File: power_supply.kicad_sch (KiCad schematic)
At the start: 37 parts, among them CON1 USB_B_Micro, CON2 Barrel_Jack_MountingPin, Q1 AO3401A, U1 AP1117-33, U2 AP6503, U3 CP2102N

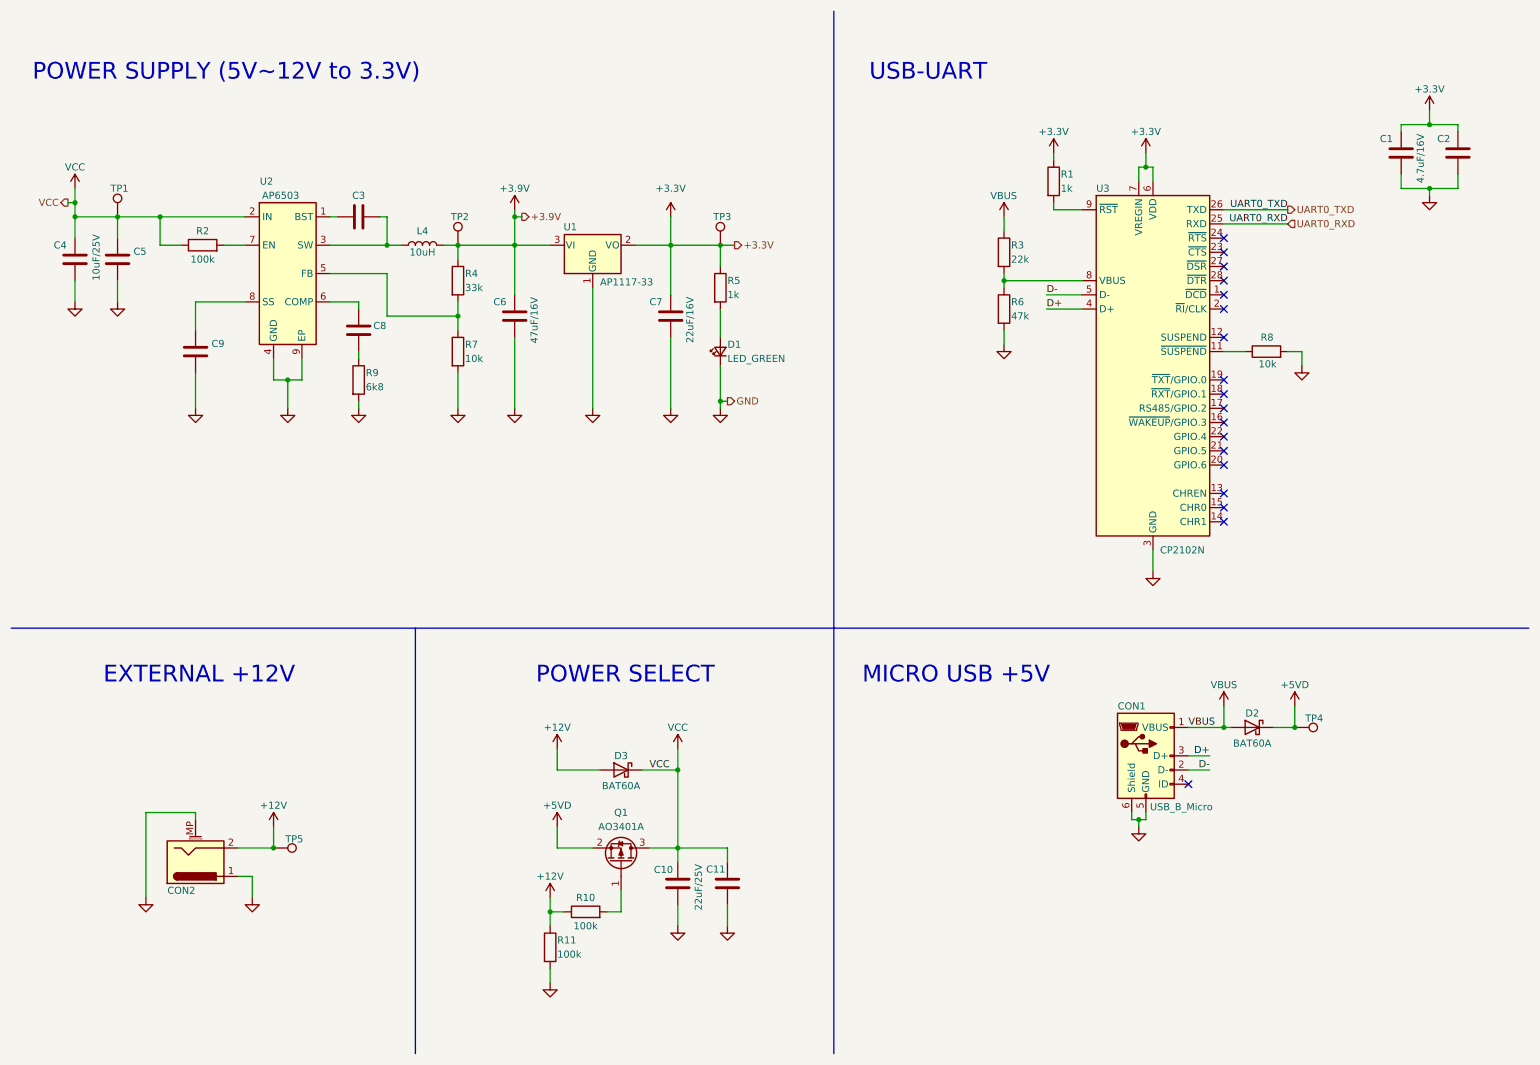
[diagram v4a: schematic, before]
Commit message: Adicionado os pads dos Test Point e alterado o Bead
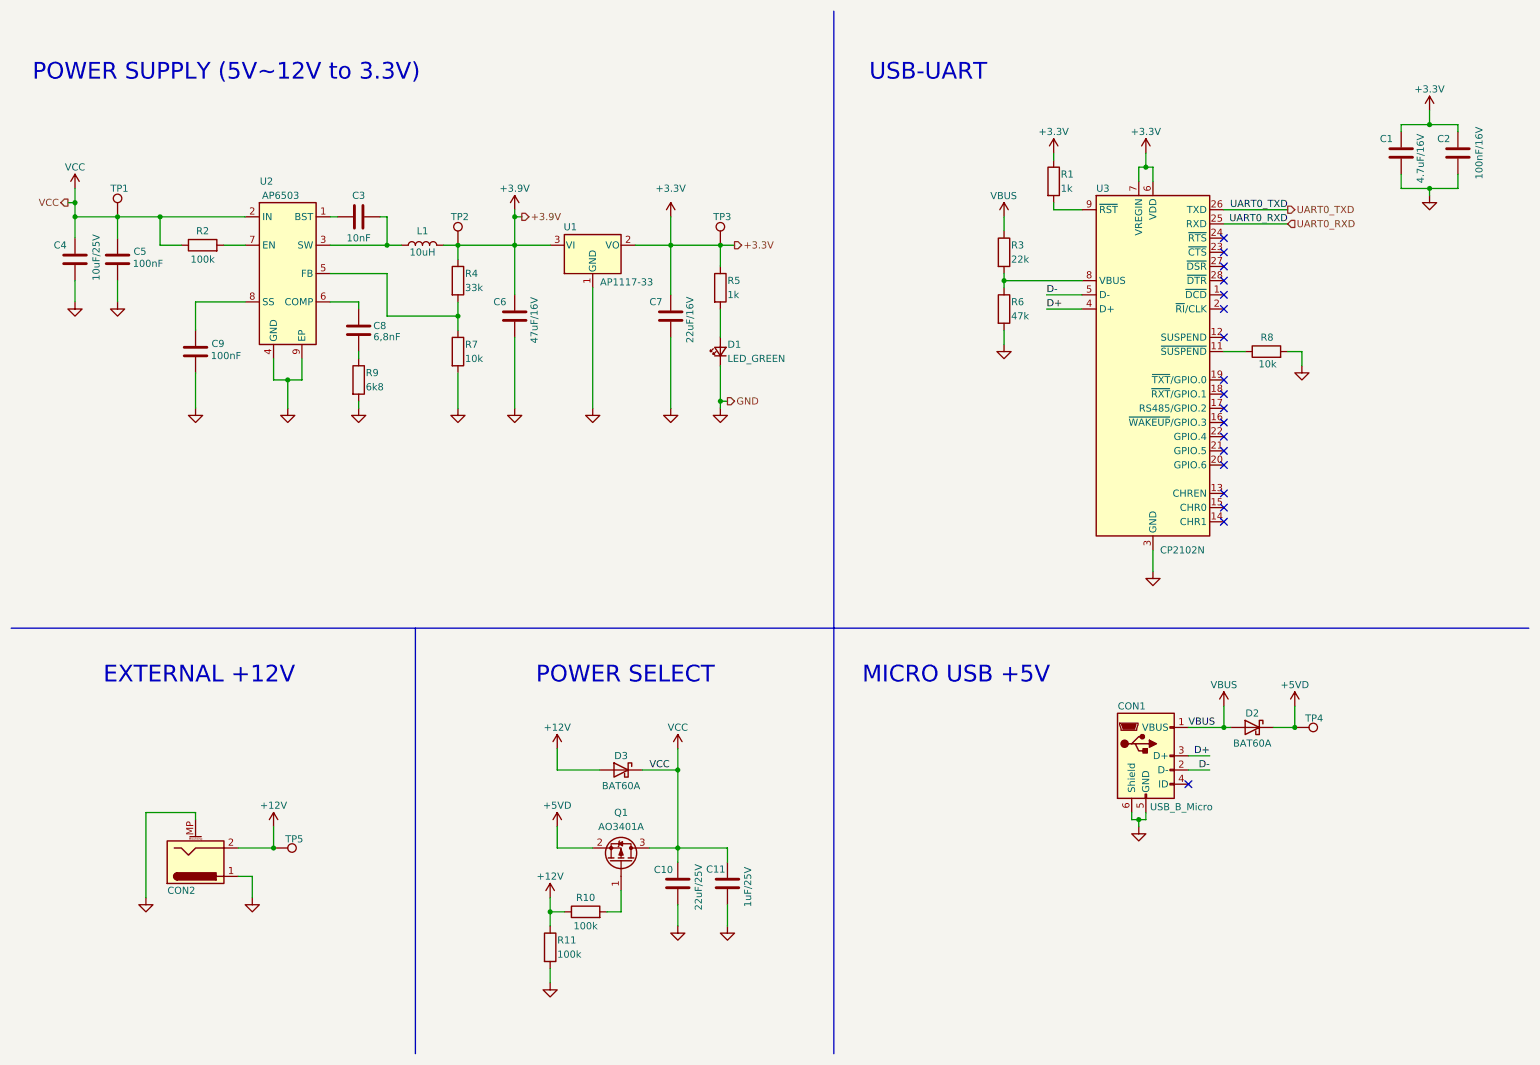
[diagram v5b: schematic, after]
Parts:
- C11: value (none) -> 1uF/25V; footprint (none) -> Capacitor_SMD:C_0603_1608Metric_Pad1.08x0.95mm_HandSolder
- C2: value (none) -> 100nF/16V; footprint (none) -> Capacitor_SMD:C_0603_1608Metric_Pad1.08x0.95mm_HandSolder
- C3: value (none) -> 10nF; footprint (none) -> Capacitor_SMD:C_0603_1608Metric_Pad1.08x0.95mm_HandSolder
- C5, C9: value (none) -> 100nF; footprint (none) -> Capacitor_SMD:C_0603_1608Metric_Pad1.08x0.95mm_HandSolder
- C8: value (none) -> 6,8nF; footprint (none) -> Capacitor_SMD:C_0603_1608Metric_Pad1.08x0.95mm_HandSolder
- TP1, TP2, TP3, TP4, TP5: value TestPoint -> (none)
- renumbered L4 to L1
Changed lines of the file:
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@@
       (effects (font (size 1.27 1.27)) (justify left))
     )
-    (property "Value" "TestPoint" (id 1) (at 142.24 51.3079 0)
+    (property "Value" "" (id 1) (at 142.24 51.3079 0)
       (effects (font (size 1.27 1.27)) (justify left) hide)
     )
@@
   (symbol (lib_id "Device:L") (at 86.36 53.34 90) (unit 1)
     (in_bom yes) (on_board yes)
-    (property "Reference" "L4" (id 0) (at 86.36 50.8 90))
+    (property "Reference" "L1" (id 0) (at 86.36 50.8 90))
     (property "Value" "10uH" (id 1) (at 86.36 54.61 90))
     (property "Footprint" "Inductor_SMD:L_Bourns-SRN8040_8x8.15mm" (id 2) (at 86.36 53.34 0)
@@
       (effects (font (size 1.27 1.27)) (justify left))
     )
-    (property "Value" "" (id 1) (at 144.632 171.8591 90)
-      (effects (font (size 1.27 1.27)) (justify left))
-    )
-    (property "Footprint" "" (id 2) (at 141.9352 171.45 0)
+    (property "Value" "1uF/25V" (id 1) (at 144.632 171.8591 90)
+      (effects (font (size 1.27 1.27)) (justify left))
+    )
+    (property "Footprint" "Capacitor_SMD:C_0603_1608Metric_Pad1.08x0.95mm_HandSolder" (id 2) (at 141.9352 171.45 0)
       (effects (font (size 1.27 1.27)) hide)
     )
@@
     (in_bom yes) (on_board yes)
     (property "Reference" "C2" (id 0) (at 269.24 34.29 0))
-    (property "Value" "" (id 1) (at 275.59 36.83 90))
-    (property "Footprint" "" (id 2) (at 270.8148 33.02 0)
+    (property "Value" "100nF/16V" (id 1) (at 275.59 36.83 90))
+    (property "Footprint" "Capacitor_SMD:C_0603_1608Metric_Pad1.08x0.95mm_HandSolder" (id 2) (at 270.8148 33.02 0)
       (effects (font (size 1.27 1.27)) hide)
     )
@@
       (effects (font (size 1.27 1.27)) (justify left))
     )
-    (property "Value" "TestPoint" (id 1) (at 34.29 46.2279 0)
+    (property "Value" "" (id 1) (at 34.29 46.2279 0)
       (effects (font (size 1.27 1.27)) (justify left) hide)
     )
@@
     (in_bom yes) (on_board yes)
     (property "Reference" "C3" (id 0) (at 74.93 44.45 90))
-    (property "Value" "" (id 1) (at 74.93 52.07 90))
-    (property "Footprint" "" (id 2) (at 78.74 47.2948 0)
+    (property "Value" "10nF" (id 1) (at 74.93 52.07 90))
+    (property "Footprint" "Capacitor_SMD:C_0603_1608Metric_Pad1.08x0.95mm_HandSolder" (id 2) (at 78.74 47.2948 0)
       (effects (font (size 1.27 1.27)) hide)
     )
@@
     (in_bom yes) (on_board yes)
     (property "Reference" "C5" (id 0) (at 35.7705 54.4674 0))
-    (property "Value" "" (id 1) (at 37.2006 56.6367 0))
-    (property "Footprint" "" (id 2) (at 30.7848 52.07 0)
+    (property "Value" "100nF" (id 1) (at 37.2006 56.6367 0))
+    (property "Footprint" "Capacitor_SMD:C_0603_1608Metric_Pad1.08x0.95mm_HandSolder" (id 2) (at 30.7848 52.07 0)
       (effects (font (size 1.27 1.27)) hide)
     )
@@
       (effects (font (size 1.27 1.27)) (justify left))
     )
-    (property "Value" "" (id 1) (at 77.5519 69.7652 0)
-      (effects (font (size 1.27 1.27)) (justify left))
-    )
-    (property "Footprint" "" (id 2) (at 75.8952 72.39 0)
+    (property "Value" "6,8nF" (id 1) (at 77.5519 69.7652 0)
+      (effects (font (size 1.27 1.27)) (justify left))
+    )
+    (property "Footprint" "Capacitor_SMD:C_0603_1608Metric_Pad1.08x0.95mm_HandSolder" (id 2) (at 75.8952 72.39 0)
       (effects (font (size 1.27 1.27)) hide)
     )
@@
       (effects (font (size 1.27 1.27)) (justify left))
     )
-    (property "Value" "TestPoint" (id 1) (at 244.6021 142.24 0)
+    (property "Value" "" (id 1) (at 244.6021 142.24 0)
       (effects (font (size 1.27 1.27)) (justify left) hide)
     )
@@
       (effects (font (size 1.27 1.27)) (justify left))
     )
-    (property "Value" "TestPoint" (id 1) (at 61.7221 163.83 0)
+    (property "Value" "" (id 1) (at 61.7221 163.83 0)
       (effects (font (size 1.27 1.27)) (justify left) hide)
     )
@@
       (effects (font (size 1.27 1.27)) (justify left))
     )
-    (property "Value" "TestPoint" (id 1) (at 95.25 51.3079 0)
+    (property "Value" "" (id 1) (at 95.25 51.3079 0)
       (effects (font (size 1.27 1.27)) (justify left) hide)
     )
@@
     (in_bom yes) (on_board yes)
     (property "Reference" "C9" (id 0) (at 49.7405 70.9774 0))
-    (property "Value" "" (id 1) (at 51.1706 73.1467 0))
-    (property "Footprint" "" (id 2) (at 44.7548 68.58 0)
-      (effects (font (size 1.27 1.27)) hide)
-    )
+    (property "Value" "100nF" (id 1) (at 51.1706 73.1467 0))
+    (property "Footprint" "Capacitor_SMD:C_0603_1608Metric_Pad1.08x0.95mm_HandSolder" (id 2) (at 44.7548 68.58 0)
+      (effects (font (size 1.27 1.27)) hide)
+    )

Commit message: Iniciando a posicionar os componentes no PCB
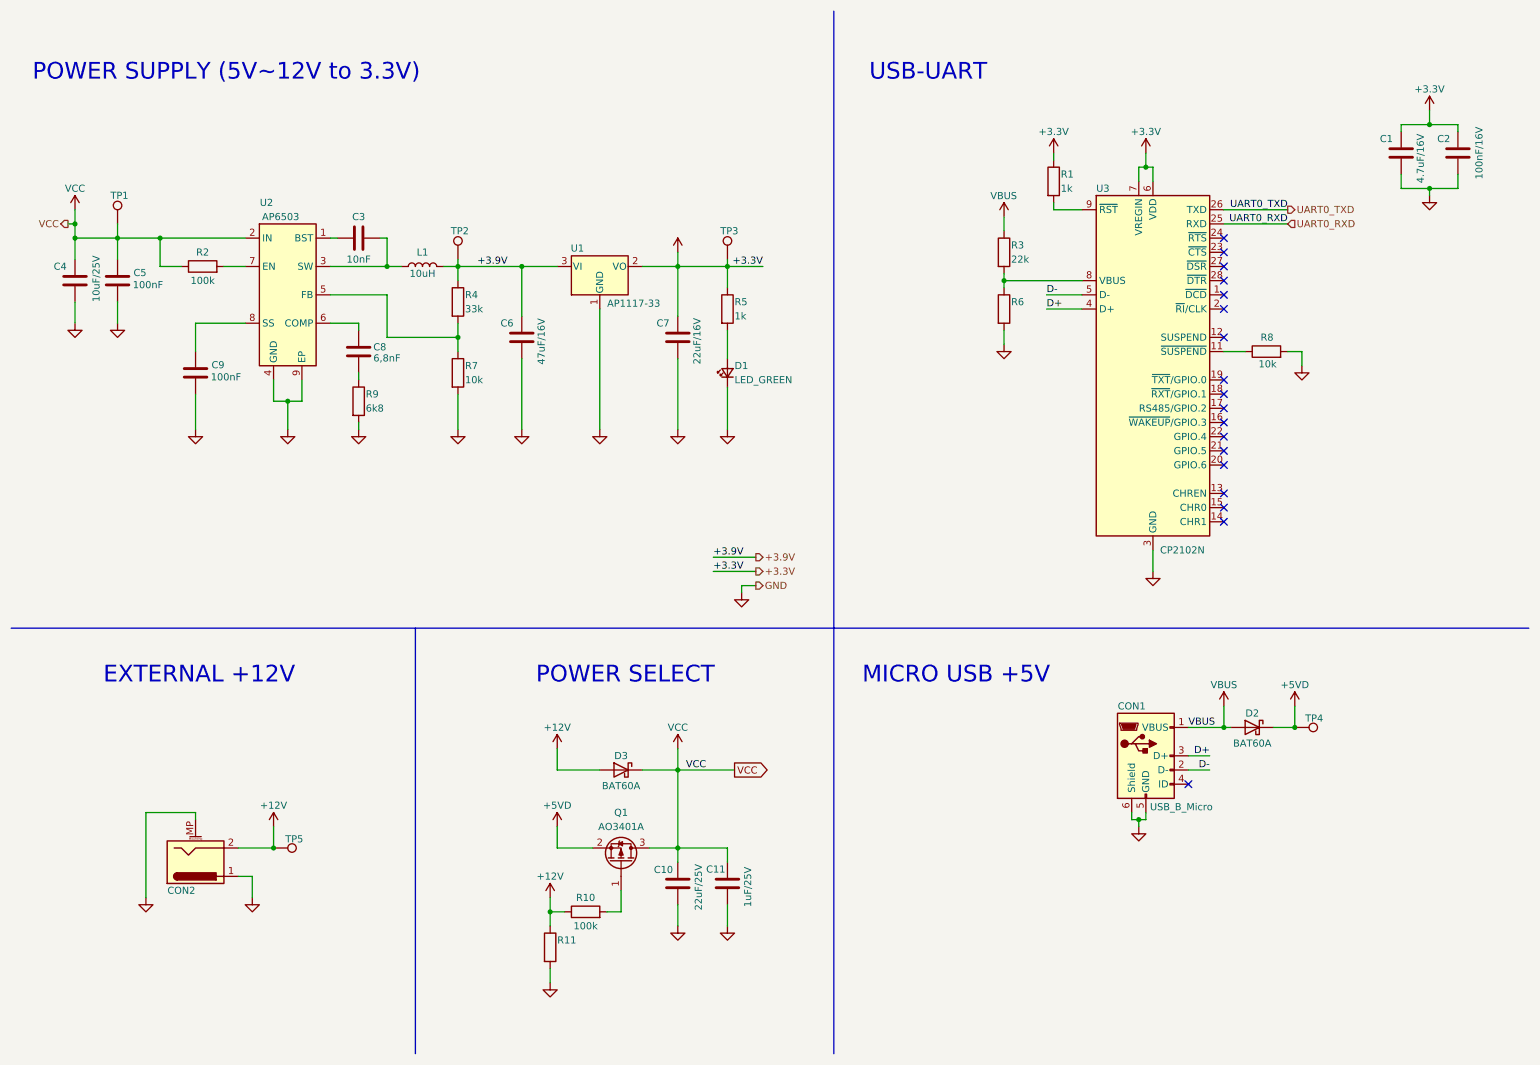
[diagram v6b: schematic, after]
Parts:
- R11: value 100k -> (none); footprint Resistor_SMD:R_0603_1608Metric_Pad0.98x0.95mm_HandSolder -> (none)
- R6: value 47k -> (none); footprint Resistor_SMD:R_0603_1608Metric_Pad0.98x0.95mm_HandSolder -> (none)
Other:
- moved on the sheet: C3, C4, C5, C6, C7, C8, C9, D1, L1, R2, R4, R5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

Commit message: Continuando com o desenvolvimento do layout
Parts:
- R6: value (none) -> 47k; footprint (none) -> Resistor_SMD:R_0603_1608Metric_Pad0.98x0.95mm_HandSolder
- TP1, TP2, TP3, TP4, TP5: value (none) -> TestPoint; footprint (none) -> TestPoint:TestPoint_Pad_1.5x1.5mm
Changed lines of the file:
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@@
       (effects (font (size 1.27 1.27)) (justify left))
     )
-    (property "Value" "" (id 1) (at 143.51 53.8479 0)
+    (property "Value" "TestPoint" (id 1) (at 143.51 53.8479 0)
       (effects (font (size 1.27 1.27)) (justify left) hide)
     )
-    (property "Footprint" "" (id 2) (at 146.05 55.88 0)
+    (property "Footprint" "TestPoint:TestPoint_Pad_1.5x1.5mm" (id 2) (at 146.05 55.88 0)
       (effects (font (size 1.27 1.27)) hide)
     )
@@
       (effects (font (size 1.27 1.27)) (justify left))
     )
-    (property "Value" "" (id 1) (at 95.25 53.8479 0)
+    (property "Value" "TestPoint" (id 1) (at 95.25 53.8479 0)
       (effects (font (size 1.27 1.27)) (justify left) hide)
     )
-    (property "Footprint" "" (id 2) (at 97.79 55.88 0)
+    (property "Footprint" "TestPoint:TestPoint_Pad_1.5x1.5mm" (id 2) (at 97.79 55.88 0)
       (effects (font (size 1.27 1.27)) hide)
     )
@@
       (effects (font (size 1.27 1.27)) (justify left))
     )
-    (property "Value" "" (id 1) (at 34.29 47.4979 0)
+    (property "Value" "TestPoint" (id 1) (at 34.29 47.4979 0)
       (effects (font (size 1.27 1.27)) (justify left) hide)
     )
-    (property "Footprint" "" (id 2) (at 36.83 49.53 0)
+    (property "Footprint" "TestPoint:TestPoint_Pad_1.5x1.5mm" (id 2) (at 36.83 49.53 0)
       (effects (font (size 1.27 1.27)) hide)
     )
@@
       (effects (font (size 1.27 1.27)) (justify left))
     )
-    (property "Value" "" (id 1) (at 244.6021 142.24 0)
+    (property "Value" "TestPoint" (id 1) (at 244.6021 142.24 0)
       (effects (font (size 1.27 1.27)) (justify left) hide)
     )
-    (property "Footprint" "" (id 2) (at 242.57 144.78 0)
+    (property "Footprint" "TestPoint:TestPoint_Pad_1.5x1.5mm" (id 2) (at 242.57 144.78 0)
       (effects (font (size 1.27 1.27)) hide)
     )
@@
       (effects (font (size 1.27 1.27)) (justify left))
     )
-    (property "Value" "" (id 1) (at 61.7221 163.83 0)
+    (property "Value" "TestPoint" (id 1) (at 61.7221 163.83 0)
       (effects (font (size 1.27 1.27)) (justify left) hide)
     )
-    (property "Footprint" "" (id 2) (at 59.69 166.37 0)
+    (property "Footprint" "TestPoint:TestPoint_Pad_1.5x1.5mm" (id 2) (at 59.69 166.37 0)
       (effects (font (size 1.27 1.27)) hide)
     )
@@
     )
     (property "Value" "" (id 1) (at 110.49 180.34 0)
-      (effects (font (size 1.27 1.27)) (justify left) hide)
+      (effects (font (size 1.27 1.27)) (justify left))
     )
     (property "Footprint" "" (id 2) (at 107.442 179.07 90)
@@
       (effects (font (size 1.27 1.27)) hide)
     )
-    (property "Value" "" (id 1) (at 132.08 50.8 0))
+    (property "Value" "+3.3V" (id 1) (at 132.08 50.8 0))
     (property "Footprint" "" (id 2) (at 132.08 54.61 0)
       (effects (font (size 1.27 1.27)) hide)
@@
       (effects (font (size 1.27 1.27)) (justify left))
     )
-    (property "Value" "" (id 1) (at 191.77 66.04 0)
-      (effects (font (size 1.27 1.27)) (justify left))
-    )
-    (property "Footprint" "" (id 2) (at 188.722 64.77 90)
-      (effects (font (size 1.27 1.27)) hide)
-    )
+    (property "Value" "47k" (id 1) (at 191.77 66.04 0)
+      (effects (font (size 1.27 1.27)) (justify left))
+    )
+    (property "Footprint" "Resistor_SMD:R_0603_1608Metric_Pad0.98x0.95mm_HandSolder" (id 2) (at 188.722 64.77 90)
+      (effects (font (size 1.27 1.27)) hide)
+    )
